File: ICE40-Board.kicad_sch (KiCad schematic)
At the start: 75 parts, among them Q1 2N222, U1 ADP1712AUJZ-3.3, U10 FT4222HQ, U2 ADP1712AUJZ-2.5, U3 ADP1712AUJZ-1.2, U4 Barrel_Jack, U5 W25X20CLSNIG, U6 USB_C_Receptacle_USB2.0, U7 ICE40HX4K-TQ144, U8 W25X20CLSNIG, U9 SIT2001BI-S2-33E-25.000000G

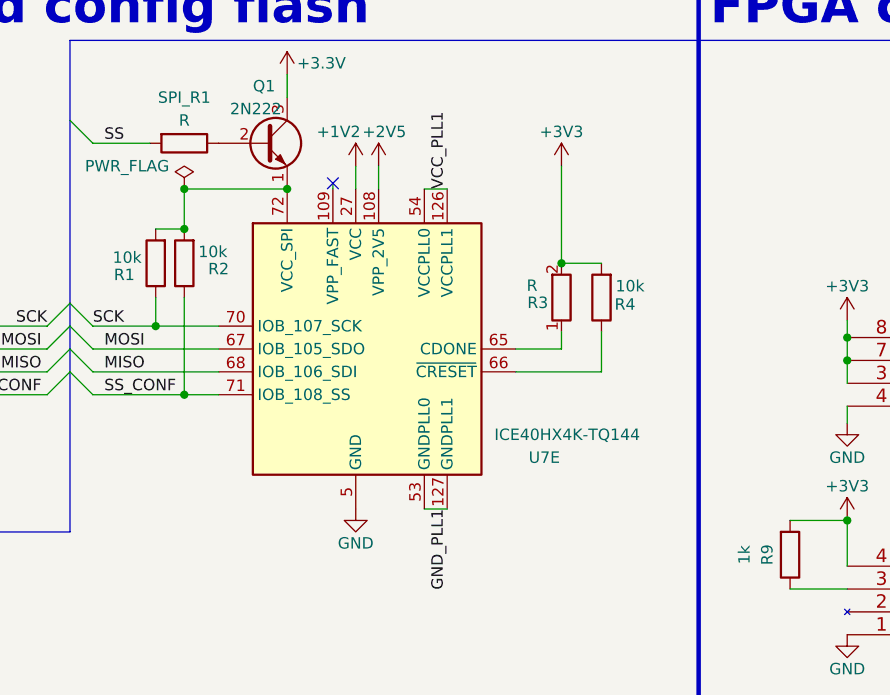
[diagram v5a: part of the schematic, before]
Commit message: USB-C routing complete
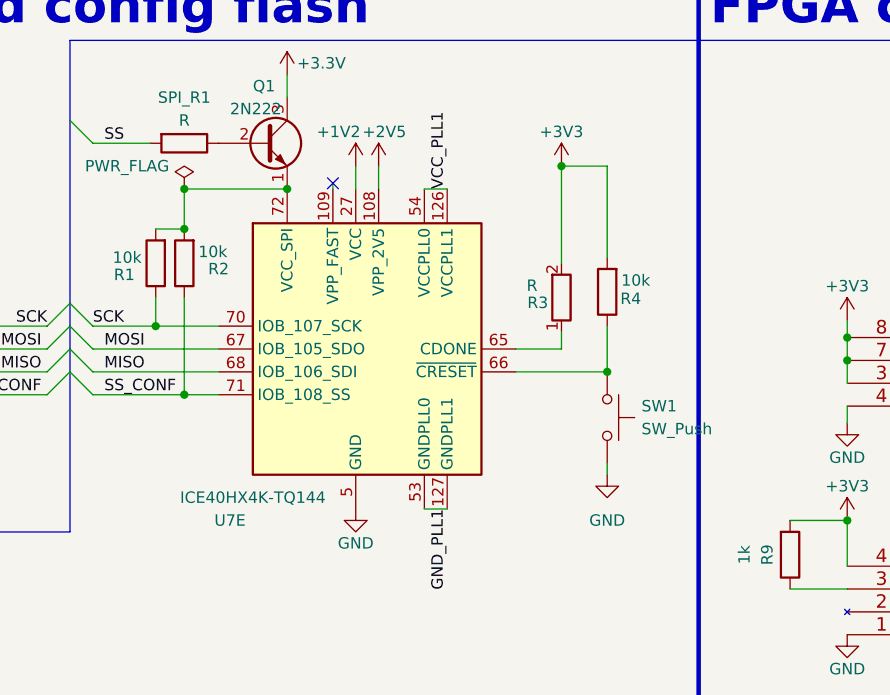
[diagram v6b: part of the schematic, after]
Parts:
- added SW1: SW_Push, Button_Switch_THT:SW_PUSH_6mm, symbol Switch:SW_Push
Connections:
- net GND: now also SW1.2
- net at R4.1, U7.66 (~{CRESET}): now also SW1.1
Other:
- moved on the sheet: R4
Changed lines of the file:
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@@
   (junction (at 358.14 118.11) (diameter 0) (color 0 0 0 0)
   )
+  (junction (at 196.85 72.39) (diameter 0) (color 0 0 0 0)
+  )
   (junction (at 77.47 194.31) (diameter 0) (color 0 0 0 0)
   )
@@
   (junction (at 154.94 74.93) (diameter 0) (color 0 0 0 0)
   )
-  (junction (at 196.85 83.185) (diameter 0) (color 0 0 0 0)
-  )
   (junction (at 344.17 110.49) (diameter 0) (color 0 0 0 0)
   )
@@
   (junction (at 45.72 86.36) (diameter 0) (color 0 0 0 0)
   )
+  (junction (at 201.93 95.25) (diameter 0) (color 0 0 0 0)
+  )
   (junction (at 365.76 100.33) (diameter 0) (color 0 0 0 0)
   )
@@
     (stroke (width 0) (type default) (color 0 0 0 0))
   )
+  (wire (pts (xy 201.93 90.17) (xy 201.93 95.25))
+    (stroke (width 0) (type default) (color 0 0 0 0))
+  )
   (wire (pts (xy 97.155 32.385) (xy 97.155 34.925))
     (stroke (width 0) (type default) (color 0 0 0 0))
@@
     (stroke (width 0) (type default) (color 0 0 0 0))
   )
+  (wire (pts (xy 201.93 106.68) (xy 201.93 105.41))
+    (stroke (width 0) (type default) (color 0 0 0 0))
+  )
   (bus (pts (xy 120.65 147.32) (xy 120.65 144.78))
     (stroke (width 0) (type default) (color 0 0 0 0))
@@
     (stroke (width 0) (type default) (color 0 0 0 0))
   )
+  (wire (pts (xy 201.93 72.39) (xy 196.85 72.39))
+    (stroke (width 0) (type default) (color 0 0 0 0))
+  )
   (wire (pts (xy 319.405 69.85) (xy 317.5 69.85))
     (stroke (width 0) (type default) (color 0 0 0 0))
@@
     (stroke (width 0) (type default) (color 0 0 0 0))
   )
+  (wire (pts (xy 201.93 82.55) (xy 201.93 72.39))
+    (stroke (width 0) (type default) (color 0 0 0 0))
+  )
   (wire (pts (xy 365.76 110.49) (xy 387.35 110.49))
     (stroke (width 0) (type default) (color 0 0 0 0))
@@
     (stroke (width 0) (type default) (color 0 0 0 0))
   )
-  (wire (pts (xy 201.295 95.25) (xy 201.295 90.805))
-    (stroke (width 0) (type default) (color 0 0 0 0))
-  )
   (wire (pts (xy 226.695 34.925) (xy 224.79 34.925))
     (stroke (width 0) (type default) (color 0 0 0 0))
@@
     (stroke (width 0) (type default) (color 0 0 0 0))
   )
-  (wire (pts (xy 196.85 83.185) (xy 201.295 83.185))
-    (stroke (width 0) (type default) (color 0 0 0 0))
-  )
   (wire (pts (xy 159.385 32.385) (xy 162.56 32.385))
     (stroke (width 0) (type default) (color 0 0 0 0))
@@
     (stroke (width 0) (type default) (color 0 0 0 0))
   )
-  (wire (pts (xy 191.77 95.25) (xy 201.295 95.25))
-    (stroke (width 0) (type default) (color 0 0 0 0))
-  )
   (wire (pts (xy 140.97 147.32) (xy 143.51 147.32))
     (stroke (width 0) (type default) (color 0 0 0 0))
@@
     (stroke (width 0) (type default) (color 0 0 0 0))
   )
+  (wire (pts (xy 201.93 95.25) (xy 191.77 95.25))
+    (stroke (width 0) (type default) (color 0 0 0 0))
+  )
   (wire (pts (xy 159.385 32.385) (xy 159.385 34.925))
     (stroke (width 0) (type default) (color 0 0 0 0))
@@
   (symbol (lib_id "FPGA_Lattice:ICE40HX4K-TQ144") (at 173.99 92.71 0) (unit 5)
     (in_bom yes) (on_board yes)
-    (property "Reference" "U7" (id 0) (at 194.945 104.775 0))
-    (property "Value" "ICE40HX4K-TQ144" (id 1) (at 197.485 102.235 0))
+    (property "Reference" "U7" (id 0) (at 160.02 111.76 0))
+    (property "Value" "ICE40HX4K-TQ144" (id 1) (at 162.56 109.22 0))
     (property "Footprint" "Package_QFP:TQFP-144_20x20mm_P0.5mm" (id 2) (at 199.39 140.97 0)
       (effects (font (size 1.27 1.27)) (justify right) hide)
@@
     (pin "2")
   )
-  (symbol (lib_id "Device:R") (at 201.295 86.995 180) (unit 1)
+  (symbol (lib_id "Device:R") (at 201.93 86.36 180) (unit 1)
     (in_bom yes) (on_board yes)
-    (property "Reference" "R4" (id 0) (at 203.9106 87.7584 0))
-    (property "Value" "10k" (id 1) (at 204.47 85.725 0))
-    (property "Footprint" "Resistor_SMD:R_0603_1608Metric_Pad0.98x0.95mm_HandSolder" (id 2) (at 203.073 86.995 90)
+    (property "Reference" "R4" (id 0) (at 204.5456 87.1234 0))
+    (property "Value" "10k" (id 1) (at 205.105 85.09 0))
+    (property "Footprint" "Resistor_SMD:R_0603_1608Metric_Pad0.98x0.95mm_HandSolder" (id 2) (at 203.708 86.36 90)
       (effects (font (size 1.27 1.27)) hide)
     )
-    (property "Datasheet" "~" (id 3) (at 201.295 86.995 0)
+    (property "Datasheet" "~" (id 3) (at 201.93 86.36 0)
       (effects (font (size 1.27 1.27)) hide)
     )
@@
     (pin "1")
   )
+  (symbol (lib_id "power:GND") (at 201.93 106.68 0) (unit 1)
+    (in_bom yes) (on_board yes) (fields_autoplaced)
+    (property "Reference" "#PWR056" (id 0) (at 201.93 113.03 0)
+      (effects (font (size 1.27 1.27)) hide)
+    )
+    (property "Value" "GND" (id 1) (at 201.93 111.76 0))
+    (property "Footprint" "" (id 2) (at 201.93 106.68 0)
+      (effects (font (size 1.27 1.27)) hide)
+    )
+    (property "Datasheet" "" (id 3) (at 201.93 106.68 0)
+      (effects (font (size 1.27 1.27)) hide)
+    )
+    (pin "1")
+  )
   (symbol (lib_id "power:PWR_FLAG") (at 154.94 74.93 0) (mirror y) (unit 1)
     (in_bom yes) (on_board yes)
@@
     (pin "5")
   )
+  (symbol (lib_id "Switch:SW_Push") (at 201.93 100.33 270) (unit 1)
+    (in_bom yes) (on_board yes) (fields_autoplaced)
+    (property "Reference" "SW1" (id 0) (at 205.74 99.0599 90)
+      (effects (font (size 1.27 1.27)) (justify left))
+    )
+    (property "Value" "SW_Push" (id 1) (at 205.74 101.5999 90)
+      (effects (font (size 1.27 1.27)) (justify left))
+    )
+    (property "Footprint" "Button_Switch_THT:SW_PUSH_6mm" (id 2) (at 207.01 100.33 0)
+      (effects (font (size 1.27 1.27)) hide)
+    )
+    (property "Datasheet" "~" (id 3) (at 207.01 100.33 0)
+      (effects (font (size 1.27 1.27)) hide)
+    )
+    (pin "1")
+    (pin "2")
+  )
   (symbol (lib_id "power:GND") (at 30.48 121.92 0) (unit 1)
     (in_bom yes) (on_board yes)
@@
       (reference "#PWR055") (unit 1) (value "VBUS") (footprint "")
     )
+    (path "/b9e83a12-812d-435d-9249-f6c0d632bb9f"
+      (reference "#PWR056") (unit 1) (value "GND") (footprint "")
+    )
     (path "/3d40ddc0-e003-4fd2-a4c0-0944b67779ca"
       (reference "#PWR060") (unit 1) (value "GND") (footprint "")
@@
       (reference "SPI_R1") (unit 1) (value "R") (footprint "Resistor_SMD:R_0603_1608Metric_Pad0.98x0.95mm_HandSolder")
     )
+    (path "/ecd4ec92-0a14-49e4-91b1-123bd414adf6"
+      (reference "SW1") (unit 1) (value "SW_Push") (footprint "Button_Switch_THT:SW_PUSH_6mm")
+    )
     (path "/ea3b8c9d-f2bf-4193-b0e7-ed2815936a1f"

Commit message: Routing buffers and flash
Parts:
- removed Q1: 2N222, Package_TO_SOT_THT:TO-92_Inline, symbol Transistor_BJT:2N3904
- removed SPI_R1: R, Resistor_SMD:R_0603_1608Metric_Pad0.98x0.95mm_HandSolder, symbol Device:R
- added C1, C3: 0.1uF, Capacitor_SMD:C_0603_1608Metric_Pad1.08x0.95mm_HandSolder, symbol Device:C
- added R13: 10k, Resistor_SMD:R_0603_1608Metric_Pad0.98x0.95mm_HandSolder, symbol Device:R
- added R18, R19, R24: 5k, Resistor_SMD:R_0603_1608Metric_Pad0.98x0.95mm_HandSolder, symbol Device:R
- added U11: 74LS125, Package_SO:TSSOP-14_4.4x5mm_P0.65mm, symbol 74xx:74LS125
- added U12: 74LS126, Package_SO:TSSOP-14_4.4x5mm_P0.65mm, symbol 74xx:74LS126
- R2: value 10k -> 5k
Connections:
- net +3V3: now also R1.2, R2.2, U7.72 (VCC_SPI), C1.1, C3.1, R13.2, R18.2, R19.2, R24.2, U11.14 (VCC), U12.13, U12.14 (VCC); no longer U10.32 (~{SS})
- net GND: now also C1.2, C3.2, U11.13, U11.7 (GND), U12.7 (GND)
- removed net MISO: H3.4 (Pin_4), JP4.2 (B), U5.2 (MISO), U7.39 (IOB_61), U7.68 (IOB_106_SDI)
- removed net MOSI: H3.3 (Pin_3), JP3.2 (B), U5.5 (MOSI), U7.38 (IOB_57), U7.67 (IOB_105_SDO)
- removed net SCK: H3.5 (Pin_5), JP2.2 (B), R1.1, U5.6 (CLK), U7.37 (IOB_56), U7.70 (IOB_107_SCK)
- net SS renamed SS_EXT
- net SS_EXT: now also R2.1, U11.1, U11.10, U11.2, U11.4, U12.1, U12.10, U12.4; no longer H2.2 (Pin_2)
- net SS_CONF renamed SS_FPGA_BUS
- net SS_FPGA_BUS: now also R19.1, U12.3; no longer R2.1, U7.71 (IOB_108_SS)
- net SS_PROG renamed SS_PROG_BUS
- net SS_PROG_BUS: now also R24.1
- new net: R1.1, U10.32 (~{SS})
- new net MISO_CONF: U12.12, U5.2 (MISO)
- new net MISO_EXT: H3.4 (Pin_4), JP4.2 (B), U11.11
- new net MISO_FPGA: U12.11, U7.68 (IOB_106_SDI)
- new net MISO_PROG: U11.12, U7.39 (IOB_61)
- new net MOSI_BUS: U11.6, U12.6, U5.5 (MOSI), U7.38 (IOB_57)
- new net MOSI_EXT: H3.3 (Pin_3), JP3.2 (B), U11.5
- new net MOSI_FPGA: U12.5, U7.67 (IOB_105_SDO)
- new net SCK_BUS: U11.8, U12.8, U5.6 (CLK), U7.37 (IOB_56)
- new net SCK_EXT: H3.5 (Pin_5), JP2.2 (B), U11.9
- new net SCK_FPGA: R13.1, U12.9, U7.70 (IOB_107_SCK)
- new net SS_EXT_BUS: H2.2 (Pin_2), U11.3
- new net SS_FPGA: R18.1, U12.2, U7.71 (IOB_108_SS)
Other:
- note added: "Buffers"
- note added: "FPGA config flash"
- note added: "FPGA power + SPI"
- note added: "Program Flash"
- note added: "SPI bus"
- note removed: "- Solder bridges allow user to use FTDI as SPI master or use an external programmer - The samer SPI interface is used to program both config flash and program flash - A jumper (FLASH_H11) is used to select whether config flash or program flash will be programmed - When programming either config or program flash the FPGA's SPI supply is switched off to avoid having two masters on the same SPI inte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"
- note removed: "FPGA clock and program flash"
- note removed: "FPGA power and config flash"
- moved on the sheet: C10, C11, C12, C13, C14, C15, C16, C18, C19, C2, C20, C21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

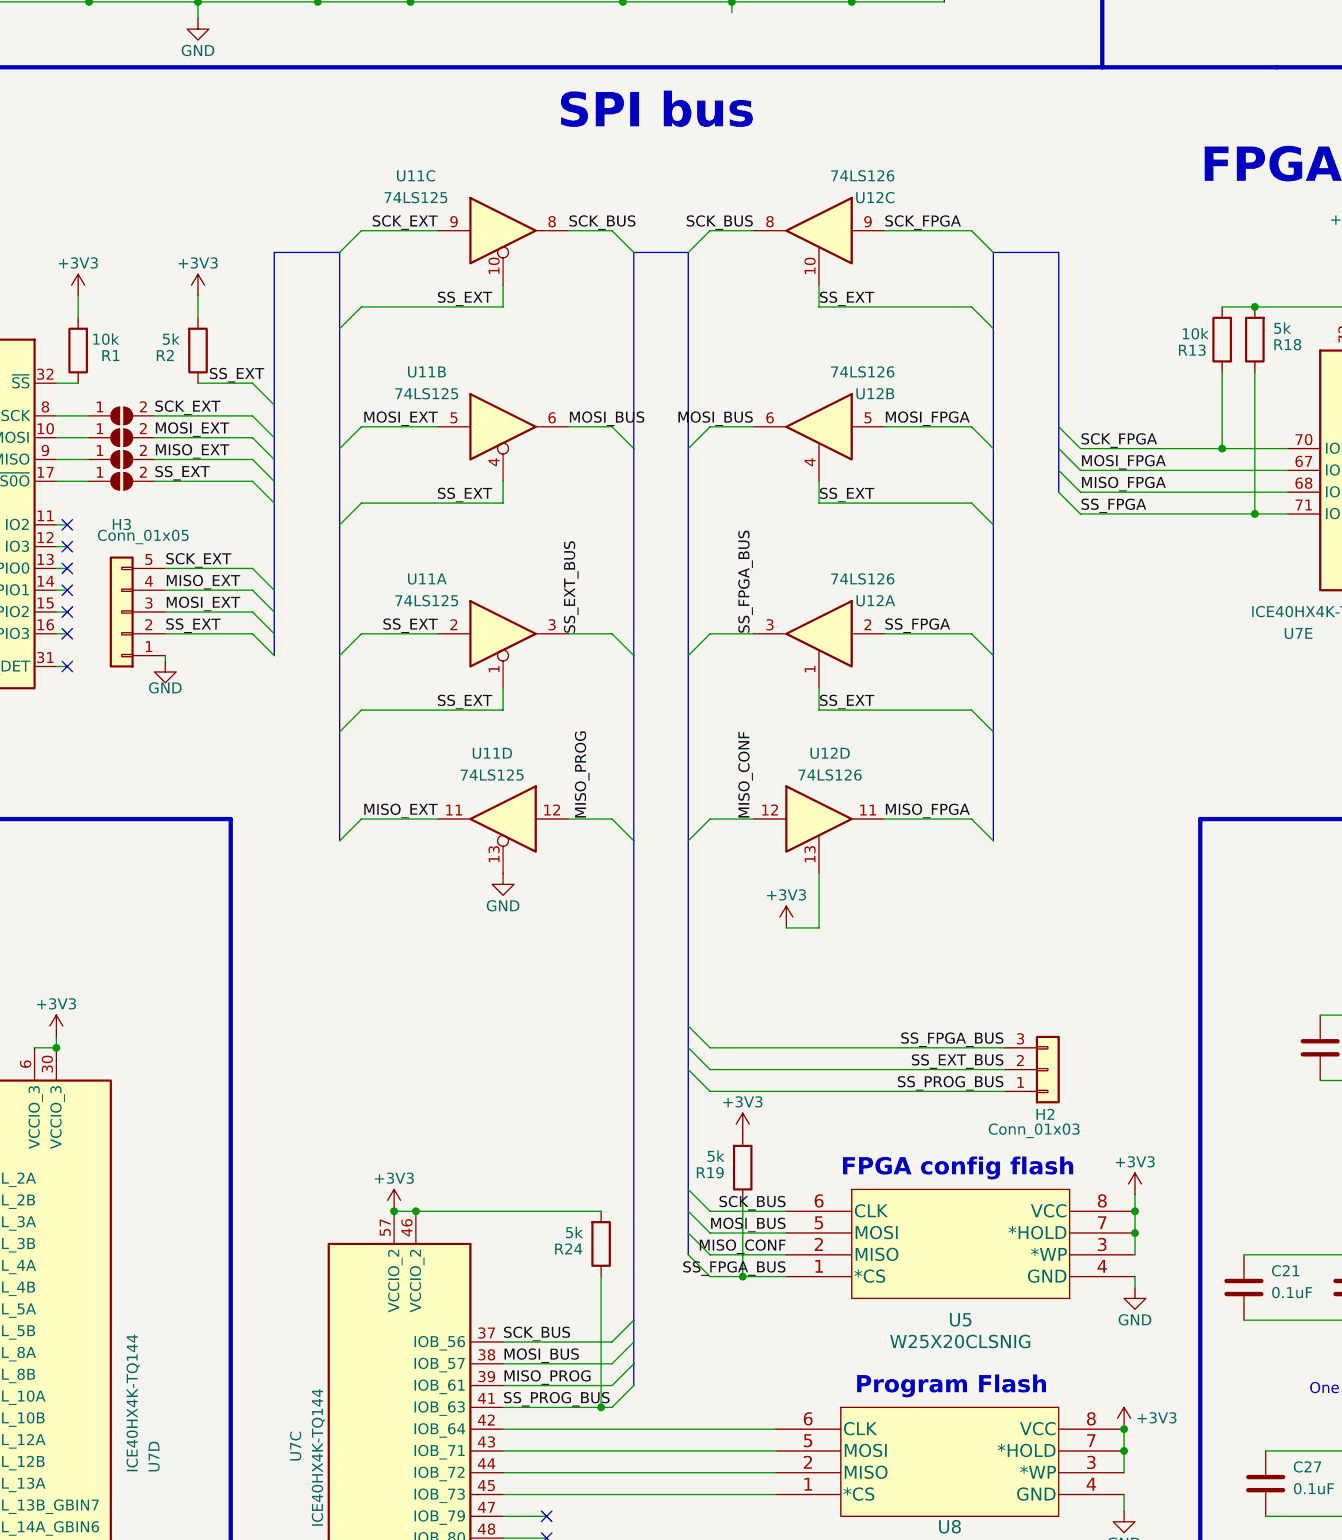
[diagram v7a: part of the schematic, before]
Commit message: Allowing MISO for both config and program flash when programming
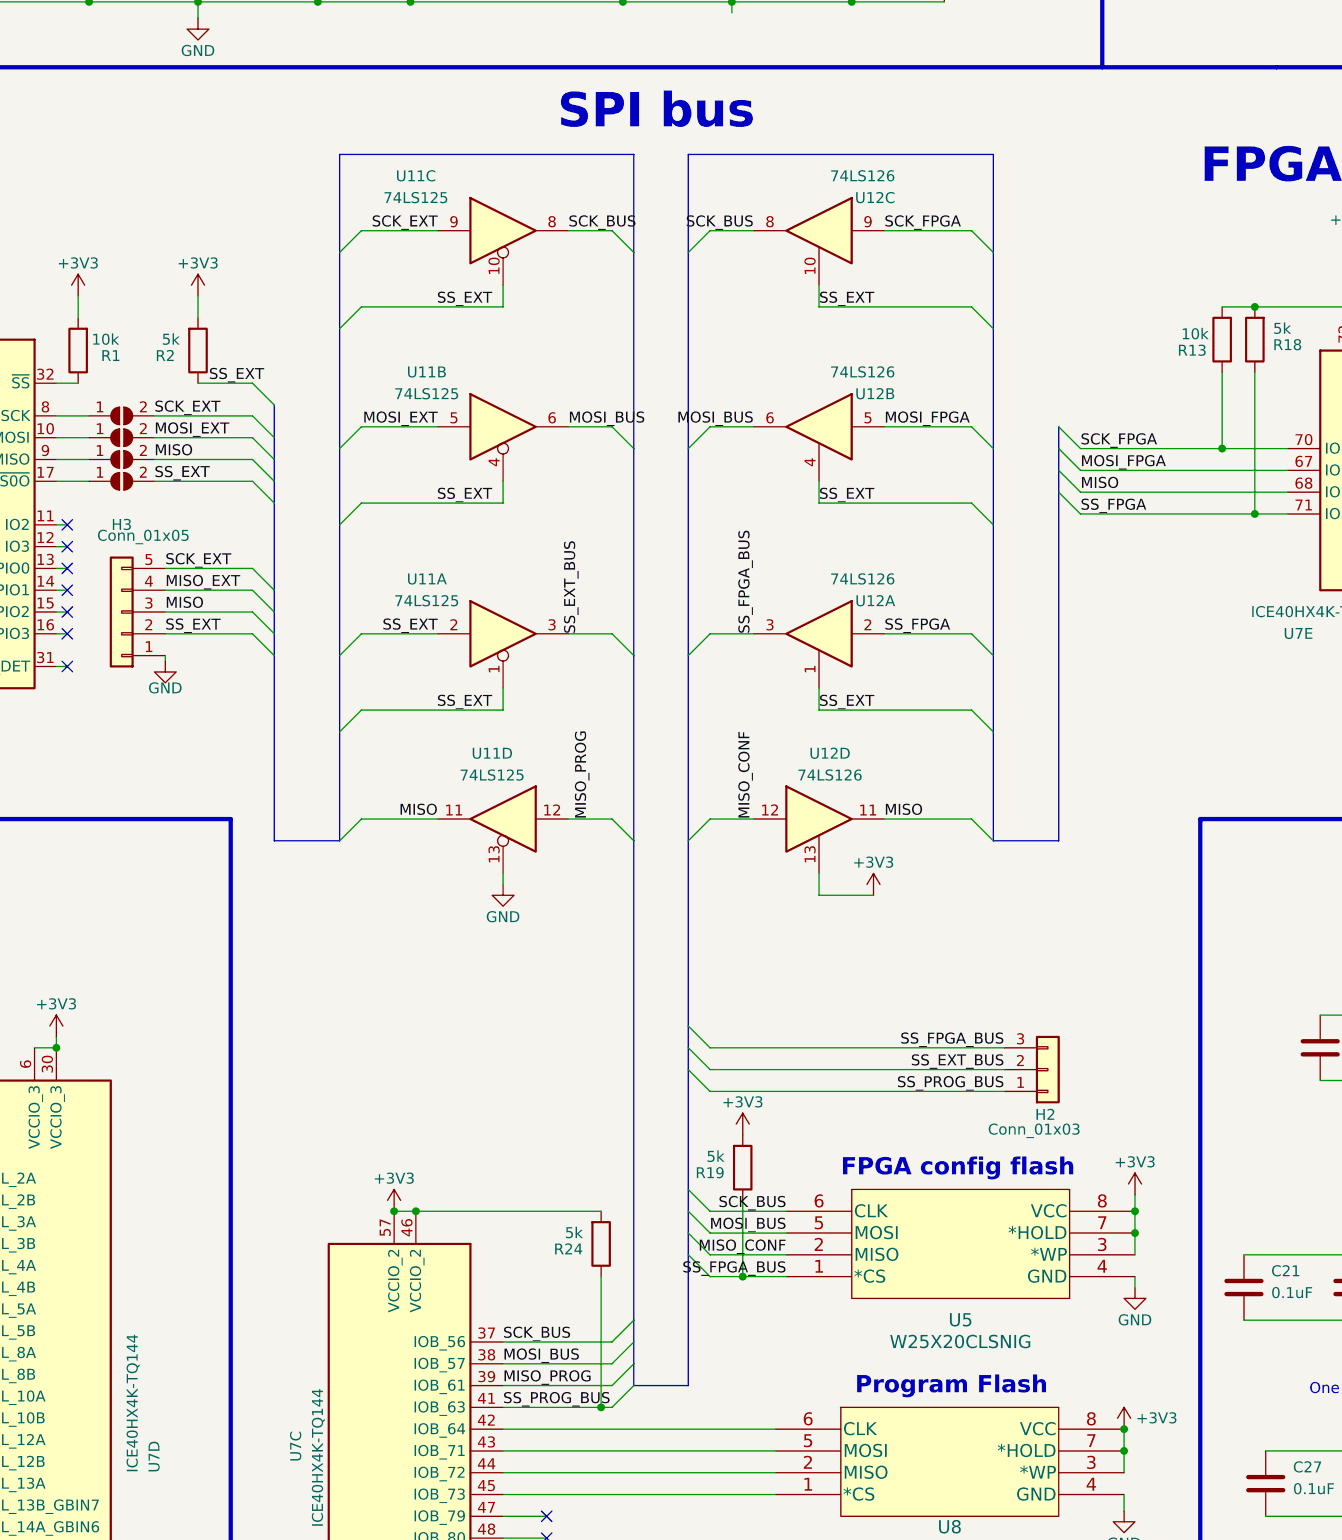
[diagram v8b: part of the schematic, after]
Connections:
- net MISO_EXT: no longer JP4.2 (B), U11.11
- net MOSI_EXT: no longer H3.3 (Pin_3)
- net MISO_FPGA renamed MISO
- net MISO: now also H3.3 (Pin_3), JP4.2 (B), U11.11
